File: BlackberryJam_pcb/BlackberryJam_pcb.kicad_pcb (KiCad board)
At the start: 2 copper layers, 10 parts, among them M2 PUMP2, M3 CONTROL GROUP MOTOR, U1 HW-107_Breakout, U2 ARDUINO PRO MINI, U3 Slip_Ring, U4 MMA8452Q, U5 MOTOR DRIVER

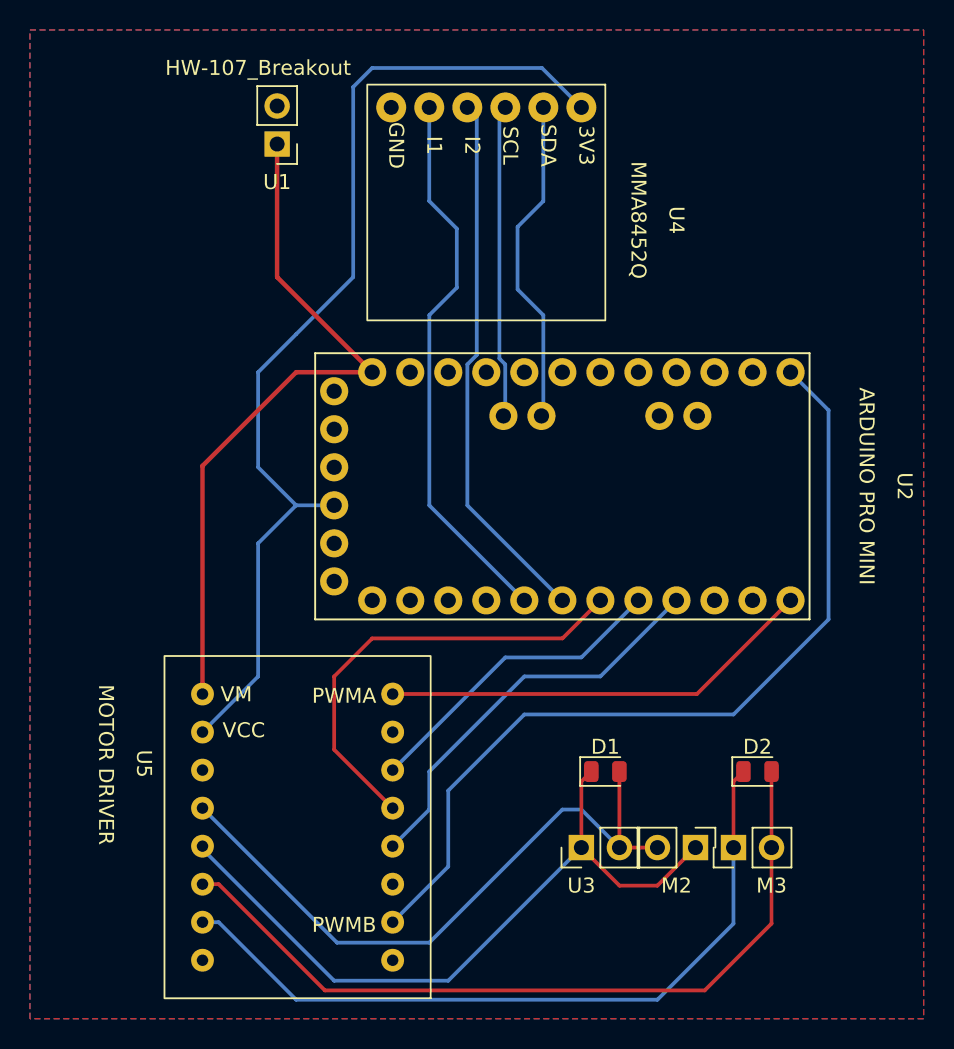
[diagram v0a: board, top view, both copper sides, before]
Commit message: Pre-Order PCB and Schematic Update
1. Updated project file directory
2. Added plated mounting hole
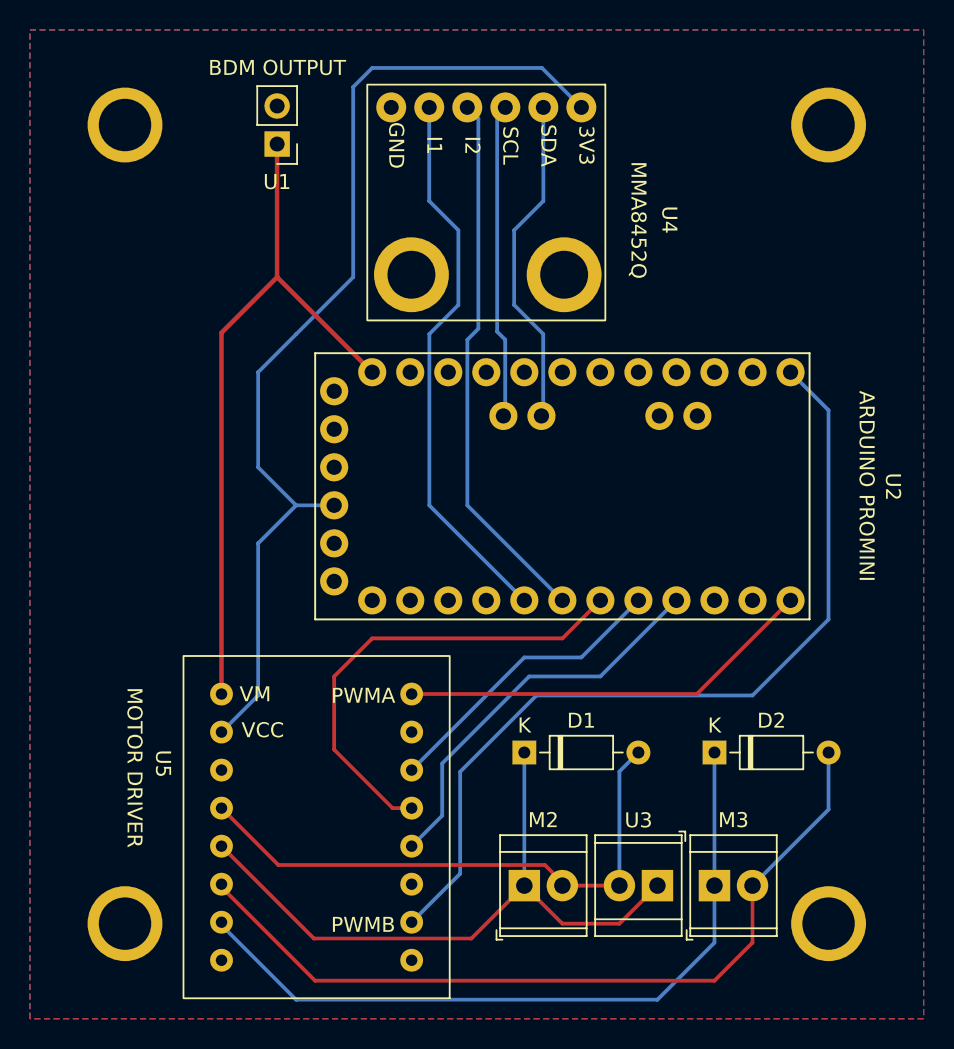
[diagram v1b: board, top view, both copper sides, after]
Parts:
- added REF**: MountingHole_3.5mm_Pad, MountingHole:MountingHole_3.5mm_Pad, F.Cu at (53.3, 6.35)
- added REF**: MountingHole_3.5mm_Pad, MountingHole:MountingHole_3.5mm_Pad, F.Cu at (6.35, 59.7)
- added REF**: MountingHole_3.5mm_Pad, MountingHole:MountingHole_3.5mm_Pad, F.Cu at (6.35, 6.35)
- added REF**: MountingHole_3.5mm_Pad, MountingHole:MountingHole_3.5mm_Pad, F.Cu at (53.3, 59.7)
- D1, D2: footprint Diode_SMD:D_0805_2012Metric -> Diode_THT:D_DO-35_SOD27_P7.62mm_Horizontal
- M2, M3, U3: footprint Connector_PinHeader_2.54mm:PinHeader_1x02_P2.54mm_Vertical -> TerminalBlock_TE-Connectivity:TerminalBlock_TE_282834-2_1x02_P2.54mm_Horizontal
- U1: value HW-107_Breakout -> BDM OUTPUT
- U2: value ARDUINO PRO MINI -> ARDUINO PROMINI
- moved M2 11.7 mm to (33.0, 57.1), turned to 0 degrees
- moved U3 5.68 mm to (41.9, 57.1), turned to 180 degrees
- moved D1 5.56 mm to (33.0, 48.3)
- moved D2 3.14 mm to (45.7, 48.3)
- moved M3 2.84 mm to (45.7, 57.1), turned to 0 degrees
- moved U5 1.27 mm to (10.3, 64.7)
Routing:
- net Net-(D1-Pad2): track 44.2 -> 38.3 mm
- net Net-(D1-Pad1): track 47.9 -> 44.1 mm
- net D5: track 21.1 -> 19.8 mm
- net D4: track 30.3 -> 31.6 mm
- net D9 (PWM): track 29.2 -> 27.9 mm
- net Net-(D2-Pad2): track 53.0 -> 54.2 mm
- net D6: track 27.2 -> 26.5 mm
- net Net-(D2-Pad1): track 50.1 -> 49.5 mm
- net VCC (3.3V): track 68.8 -> 68.2 mm
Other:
- board text added: "JLCJLCJLCJLC"

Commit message: PCB Update - Production
1. Final check on footprint and clearance of traces on PCB
2. Generated production files (.gbr & .drl)

*PCB is ordered with this update
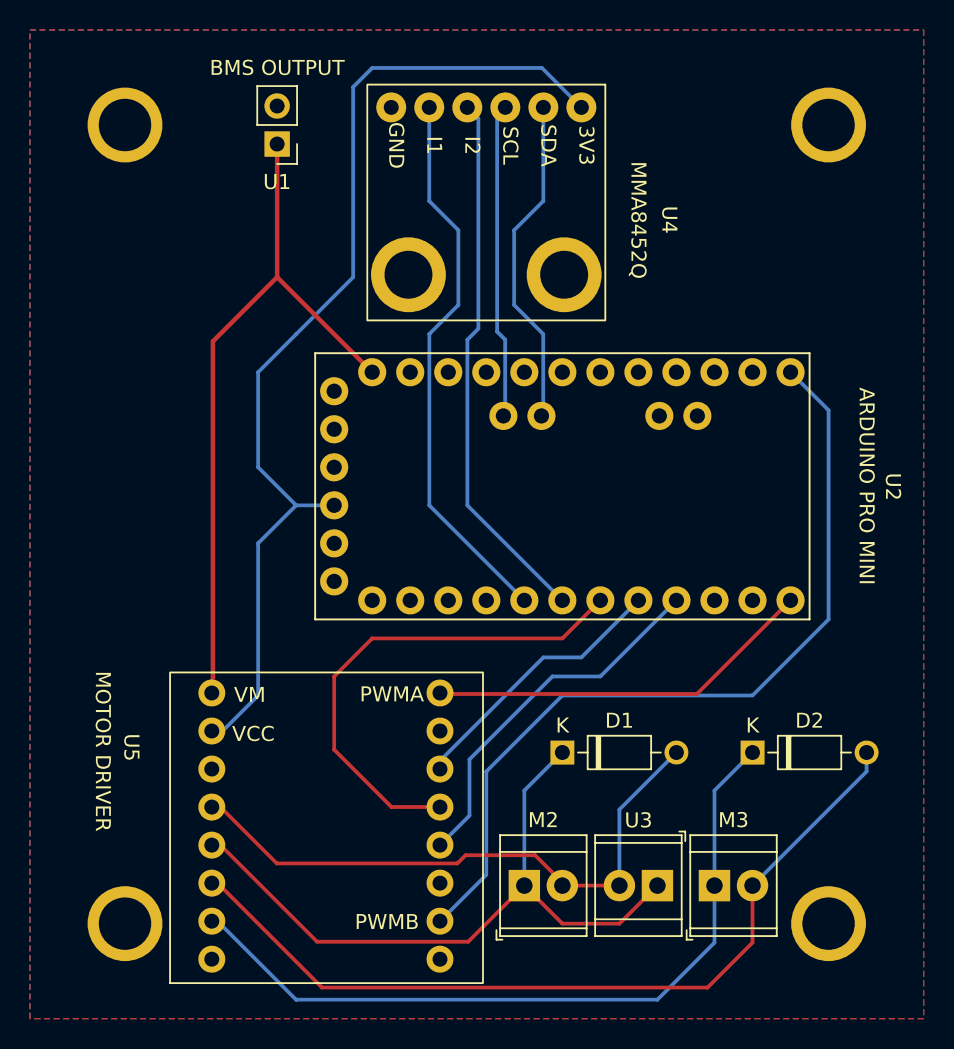
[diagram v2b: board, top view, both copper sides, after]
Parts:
- U1: value BDM OUTPUT -> BMS OUTPUT
- U2: value ARDUINO PROMINI -> ARDUINO PRO MINI
- moved U5 3.22 mm to (12.1, 62.1)
- moved D1 2.54 mm to (35.6, 48.3)
- moved D2 2.54 mm to (48.3, 48.3)
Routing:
- net D10 (PWM): track 57.8 -> 55.9 mm
- net D9 (PWM): track 27.9 -> 26.0 mm
- net D4: track 31.6 -> 33.4 mm
- net D6: track 26.5 -> 24.8 mm
- net D5: track 19.8 -> 18.2 mm
- net Net-(D1-Pad2): track 38.3 -> 39.8 mm
- net Net-(D2-Pad2): track 54.2 -> 55.6 mm
- net Net-(D1-Pad1): track 44.1 -> 45.4 mm
- net Net-(D2-Pad1): track 49.5 -> 50.6 mm

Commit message: Updated PCB Routing after Testing
1. Added GROUND and VCC wiring
2. Ran DRC
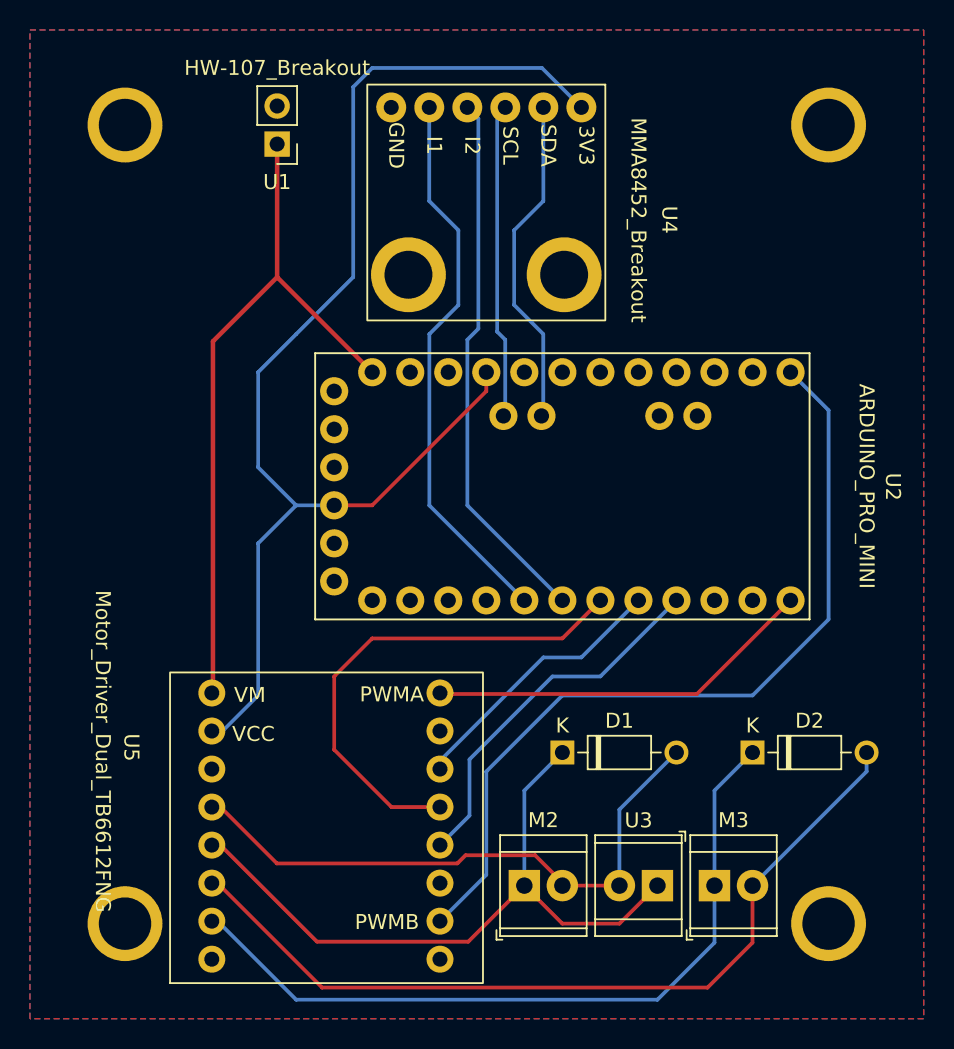
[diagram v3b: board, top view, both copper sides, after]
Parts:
- U1: value BMS OUTPUT -> HW-107_Breakout
- U2: value ARDUINO PRO MINI -> ARDUINO_PRO_MINI
- U4: value MMA8452Q -> MMA8452_Breakout
- U5: value MOTOR DRIVER -> Motor_Driver_Dual_TB6612FNG
- UVR 2022 XENIA-1 : renamed from HVR 2022 XENIA-1 
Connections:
- U2 pad JP6_2: unconnected-(U2-PadJP6_2) -> GND
- U2 pad JP6_4: unconnected-(U2-PadJP6_4) -> VCC (3.3V)
- U2 pad JP7_9: unconnected-(U2-PadJP7_9) -> GND
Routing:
- net VCC (3.3V): track 68.2 -> 82.8 mm
